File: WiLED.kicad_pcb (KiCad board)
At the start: 2 copper layers, 36.6 x 82.3 mm, 54 parts, among them P1 Serial to USB, P2 DC In, P3 Lamp Connector, P4 LED Out, SW1 Reset, SW2 Boot, SW3 Toggle, SW4 Rotary Encoder, U1 ESP-WROOM-32, U2 VXO7803-500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

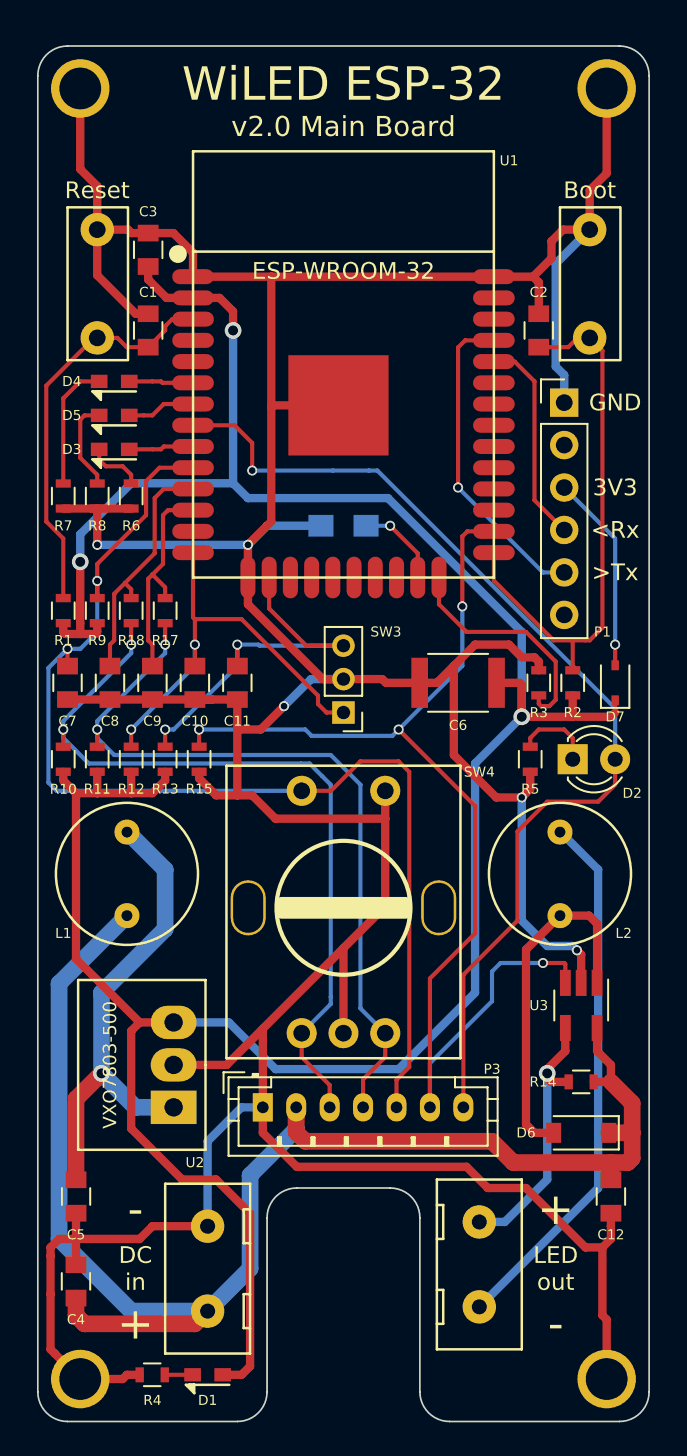
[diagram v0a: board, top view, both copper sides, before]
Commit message: Add ground copper pours
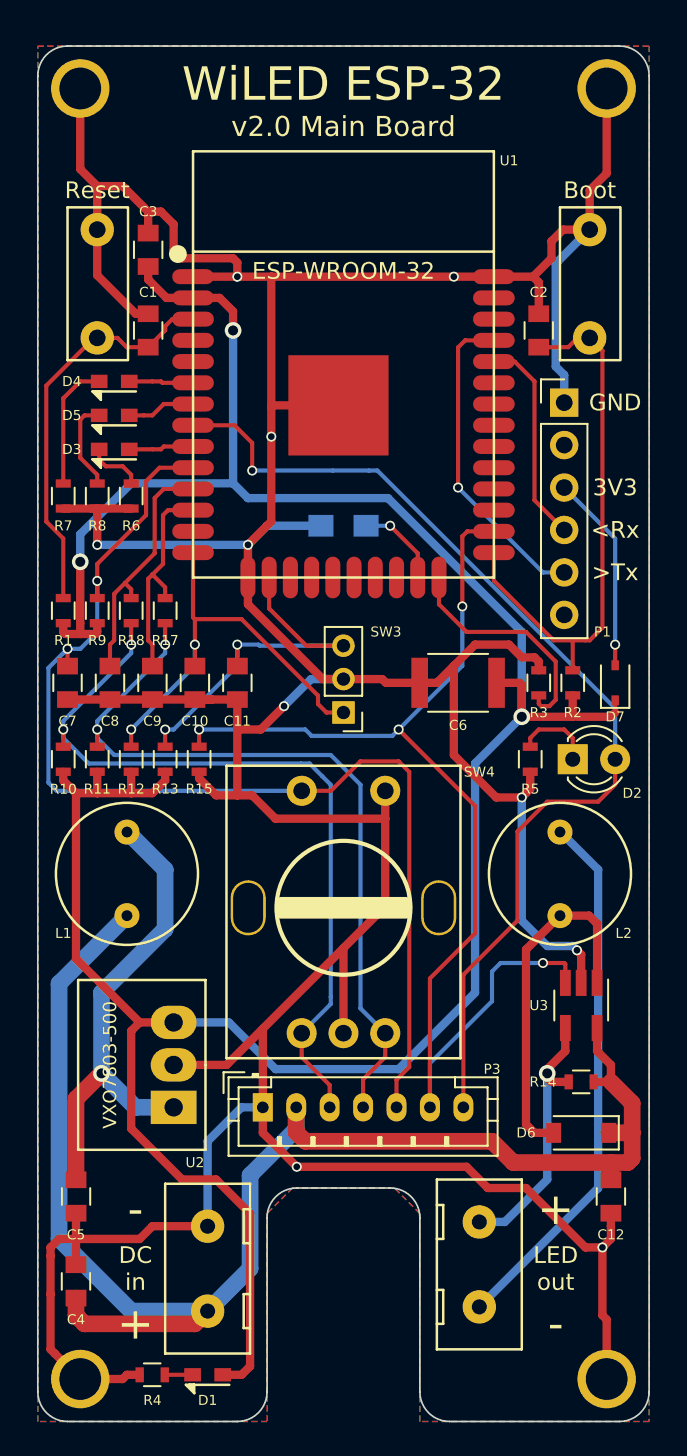
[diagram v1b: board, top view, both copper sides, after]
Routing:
- net GND: track 303.1 -> 308.8 mm, vias 5 -> 10
- added copper zone on B.Cu, net GND
- added copper zone on F.Cu, net GND
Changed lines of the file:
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@@
     (links 107)
     (no_connects 0)
-    (area 152.733905 50.414 193.25362 135.868)
+    (area 154.381999 52.019999 191.058001 134.416001)
     (thickness 1.6)
     (drawings 36)
-    (tracks 493)
+    (tracks 509)
     (zones 0)
     (modules 54)
@@
     (trace_clearance 0.25)
     (zone_clearance 0.508)
-    (zone_45_only no)
+    (zone_45_only yes)
     (trace_min 0.25)
     (segment_width 0.2)
@@
     (pad_drill 2.5)
     (pad_to_mask_clearance 0)
-    (aux_axis_origin 0 0)
+    (aux_axis_origin 154.432 52.07)
     (visible_elements FFFFFF7F)
     (pcbplotparams
-      (layerselection 0x00030_80000001)
-      (usegerberextensions false)
+      (layerselection 0x010f8_80000001)
+      (usegerberextensions true)
       (excludeedgelayer true)
       (linewidth 0.100000)
@@
       (outputformat 1)
       (mirror false)
-      (drillshape 1)
+      (drillshape 0)
       (scaleselection 1)
-      (outputdirectory ""))
+      (outputdirectory gerber/))
   )
   (net 0 "")
@@
   (segment (start 162.052 68.834) (end 162.052 69.072) (width 0.25) (layer F.Cu) (net 1))
   (segment (start 162.052 69.072) (end 161.036 70.088) (width 0.25) (layer F.Cu) (net 1))
+  (via (at 166.37 65.87) (size 0.6) (drill 0.4) (layers F.Cu B.Cu) (net 2))
+  (segment (start 166.3446 65.913) (end 166.3446 65.8954) (width 0.5) (layer B.Cu) (net 2))
+  (segment (start 166.3446 65.8954) (end 166.37 65.87) (width 0.5) (layer B.Cu) (net 2))
+  (via (at 179.324 65.87) (size 0.6) (drill 0.4) (layers F.Cu B.Cu) (net 2))
+  (segment (start 179.2986 65.8368) (end 179.2986 65.8446) (width 0.5) (layer B.Cu) (net 2))
+  (segment (start 179.2986 65.8446) (end 179.324 65.87) (width 0.5) (layer B.Cu) (net 2))
+  (via (at 168.402 75.438) (size 0.6) (drill 0.4) (layers F.Cu B.Cu) (net 2))
+  (via (at 169.926 119.126) (size 0.6) (drill 0.4) (layers F.Cu B.Cu) (net 2))
+  (via (at 188.214 123.952) (size 0.6) (drill 0.4) (layers F.Cu B.Cu) (net 2))
+  (segment (start 166.37 65.87) (end 166.37 65.024) (width 0.5) (layer F.Cu) (net 2))
+  (segment (start 161.798 61.976) (end 161.036 61.976) (width 0.5) (layer F.Cu) (net 2))
+  (segment (start 162.56 62.738) (end 161.798 61.976) (width 0.5) (layer F.Cu) (net 2))
+  (segment (start 162.56 64.262) (end 162.56 62.738) (width 0.5) (layer F.Cu) (net 2))
+  (segment (start 163.068 64.77) (end 162.56 64.262) (width 0.5) (layer F.Cu) (net 2))
+  (segment (start 166.116 64.77) (end 163.068 64.77) (width 0.5) (layer F.Cu) (net 2))
+  (segment (start 166.37 65.024) (end 166.116 64.77) (width 0.5) (layer F.Cu) (net 2))
+  (segment (start 161.036 63.262) (end 161.036 61.976) (width 0.5) (layer F.Cu) (net 2))
+  (segment (start 159.512 60.452) (end 157.988 60.452) (width 0.5) (layer F.Cu) (net 2))
+  (segment (start 161.036 61.976) (end 159.512 60.452) (width 0.5) (layer F.Cu) (net 2))
   (segment (start 187.452 63.0555) (end 187.452 60.706) (width 0.5) (layer F.Cu) (net 2))
   (segment (start 188.468 59.69) (end 188.468 54.61) (width 0.5) (layer F.Cu) (net 2))
@@
   (segment (start 172.72 106.045) (end 172.72 111.132) (width 0.5) (layer F.Cu) (net 2))
   (segment (start 167.005 83.87) (end 167.005 81.915) (width 0.5) (layer F.Cu) (net 2))
-  (segment (start 168.402 80.518) (end 168.402 73.66) (width 0.5) (layer F.Cu) (net 2))
+  (segment (start 168.402 80.518) (end 168.402 75.438) (width 0.5) (layer F.Cu) (net 2))
+  (segment (start 168.402 75.438) (end 168.402 73.66) (width 0.5) (layer F.Cu) (net 2))
   (segment (start 168.402 73.66) (end 168.402 65.87) (width 0.5) (layer F.Cu) (net 2))
   (segment (start 167.005 81.915) (end 168.402 80.518) (width 0.5) (layer F.Cu) (net 2))
@@
   (segment (start 157.988 65.786) (end 157.988 63.0555) (width 0.5) (layer F.Cu) (net 2))
   (segment (start 160.29 68.088) (end 157.988 65.786) (width 0.5) (layer F.Cu) (net 2))
-  (segment (start 161.036 63.262) (end 162.544 63.262) (width 0.5) (layer F.Cu) (net 2))
-  (segment (start 163.72 64.438) (end 163.72 65.87) (width 0.5) (layer F.Cu) (net 2))
-  (segment (start 162.544 63.262) (end 163.72 64.438) (width 0.5) (layer F.Cu) (net 2))
-  (segment (start 161.036 63.262) (end 160.036 63.262) (width 0.5) (layer F.Cu) (net 2))
-  (segment (start 159.8295 63.0555) (end 157.988 63.0555) (width 0.5) (layer F.Cu) (net 2))
-  (segment (start 160.036 63.262) (end 159.8295 63.0555) (width 0.5) (layer F.Cu) (net 2))
   (segment (start 181.72 65.87) (end 184.066 65.87) (width 0.5) (layer F.Cu) (net 2))
   (segment (start 185.8645 63.0555) (end 187.706 63.0555) (width 0.5) (layer F.Cu) (net 2))
@@
   (segment (start 185.166 64.77) (end 185.166 63.754) (width 0.5) (layer F.Cu) (net 2))
   (segment (start 184.066 65.87) (end 185.166 64.77) (width 0.5) (layer F.Cu) (net 2))
-  (segment (start 163.72 65.87) (end 168.402 65.87) (width 0.5) (layer F.Cu) (net 2))
-  (segment (start 168.402 65.87) (end 181.72 65.87) (width 0.5) (layer F.Cu) (net 2))
+  (segment (start 163.72 65.87) (end 166.37 65.87) (width 0.5) (layer F.Cu) (net 2))
+  (segment (start 166.37 65.87) (end 168.402 65.87) (width 0.5) (layer F.Cu) (net 2))
+  (segment (start 168.402 65.87) (end 179.324 65.87) (width 0.5) (layer F.Cu) (net 2))
+  (segment (start 179.324 65.87) (end 181.72 65.87) (width 0.5) (layer F.Cu) (net 2))
   (segment (start 157.988 79.744) (end 160.02 79.744) (width 0.5) (layer F.Cu) (net 2))
   (segment (start 155.956 79.744) (end 157.988 79.744) (width 0.5) (layer F.Cu) (net 2))
@@
   (segment (start 175.22 111.085) (end 175.22 111.132) (width 0.25) (layer B.Cu) (net 51))
   (segment (start 175.22 111.132) (end 175.22 111.085) (width 0.25) (layer B.Cu) (net 51))
+  (zone (net 0) (net_name "") (layer F.Cu) (hatch edge 0.508)
+    (connect_pads (clearance 0.508))
+    (min_thickness 0.254)
+    (keepout (tracks not_allowed) (vias not_allowed) (copperpour not_allowed))
+    (fill (arc_segments 16) (thermal_gap 0.508) (thermal_bridge_width 0.508))
+    (polygon
+      (pts
+        (xy 182.118 64.516) (xy 163.322 64.516) (xy 163.322 52.578) (xy 182.118 52.578)
+      )
+    )
+  )
+  (zone (net 0) (net_name "") (layer B.Cu) (hatch edge 0.508)
+    (connect_pads (clearance 0.508))
+    (min_thickness 0.254)
+    (keepout (tracks not_allowed) (vias not_allowed) (copperpour not_allowed))
+    (fill (arc_segments 16) (thermal_gap 0.508) (thermal_bridge_width 0.508))
+    (polygon
+      (pts
+        (xy 182.118 64.516) (xy 163.322 64.516) (xy 163.322 52.578) (xy 182.118 52.578)
+      )
+    )
+  )
+  (zone (net 2) (net_name GND) (layer B.Cu) (hatch edge 0.508)
+    (connect_pads yes (clearance 0.508))
+    (min_thickness 0.254)
+    (fill yes (arc_segments 32) (thermal_gap 0.508) (thermal_bridge_width 0.508) (smoothing chamfer))
+    (polygon
+      (pts
+        (xy 191.008 134.366) (xy 177.292 134.366) (xy 177.292 121.92) (xy 175.768 120.396) (xy 169.672 120.396)
+        (xy 168.148 121.92) (xy 168.148 134.366) (xy 154.432 134.366) (xy 154.432 52.07) (xy 191.008 52.07)
+      )
+    )
+  )
+  (zone (net 2) (net_name GND) (layer F.Cu) (hatch edge 0.508)
+    (connect_pads yes (clearance 0.508))
+    (min_thickness 0.254)
+    (fill yes (arc_segments 32) (thermal_gap 0.508) (thermal_bridge_width 0.508) (smoothing chamfer))
+    (polygon
+      (pts
+        (xy 191.008 134.366) (xy 177.292 134.366) (xy 177.292 121.92) (xy 175.768 120.396) (xy 169.672 120.396)
+        (xy 168.148 121.92) (xy 168.148 134.366) (xy 154.432 134.366) (xy 154.432 52.07) (xy 191.008 52.07)
+      )
+    )
+  )
 )

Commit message: Increase via size and mounting hole size
Vias were 0.4/0.6 mm, this has been increased to 0.4/0.8 mm to make
manufacturing a little easier - and there's no reason to need the
smaller size.
The mounting holes were M2.5 size, but changed this to M3 for slightly
more standard screw fittings.
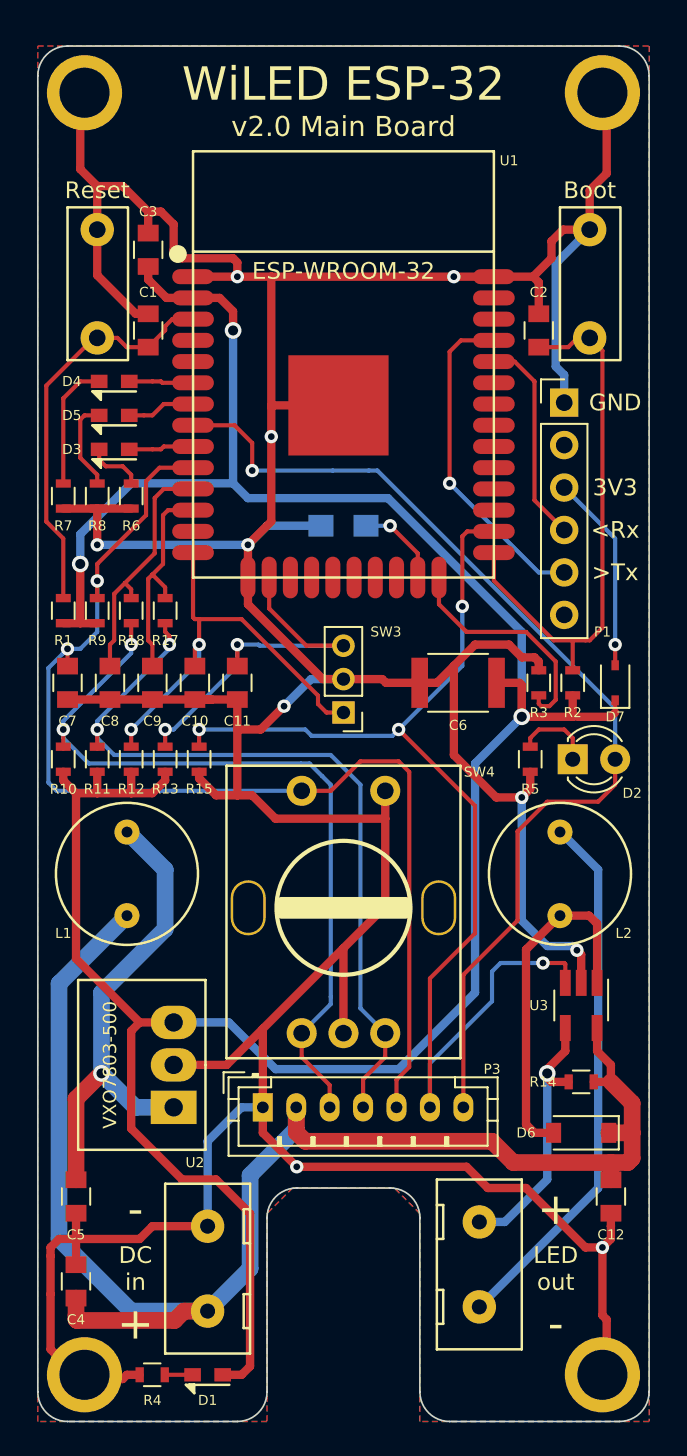
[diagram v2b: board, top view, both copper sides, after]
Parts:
- REF** (x4): footprint custom-footprints:M2.5_hole -> custom-footprints:M3_hole
- moved REF** 0.36 mm to (188.2, 54.9)
- moved REF** 0.36 mm to (157.2, 54.9)
- moved REF** 0.36 mm to (157.2, 131.6)
- moved REF** 0.36 mm to (188.2, 131.6)
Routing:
- net +3V3: track 166.9 -> 165.1 mm
- net TX: track 19.2 -> 19.9 mm
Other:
- net class Default: via_dia 0.6 -> 0.8
- net class GND: via_dia 0.6 -> 0.8
- rule via_min_drill: 0.3 -> 0.4
- rule via_min_size: 0.4 -> 0.7

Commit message: Rework LED constant-current PCB layout
Previously there were unnecssarily long traces between high-power
components in the buck-mode LED driver, this commit brings a modified
layout that tries to improve on this.
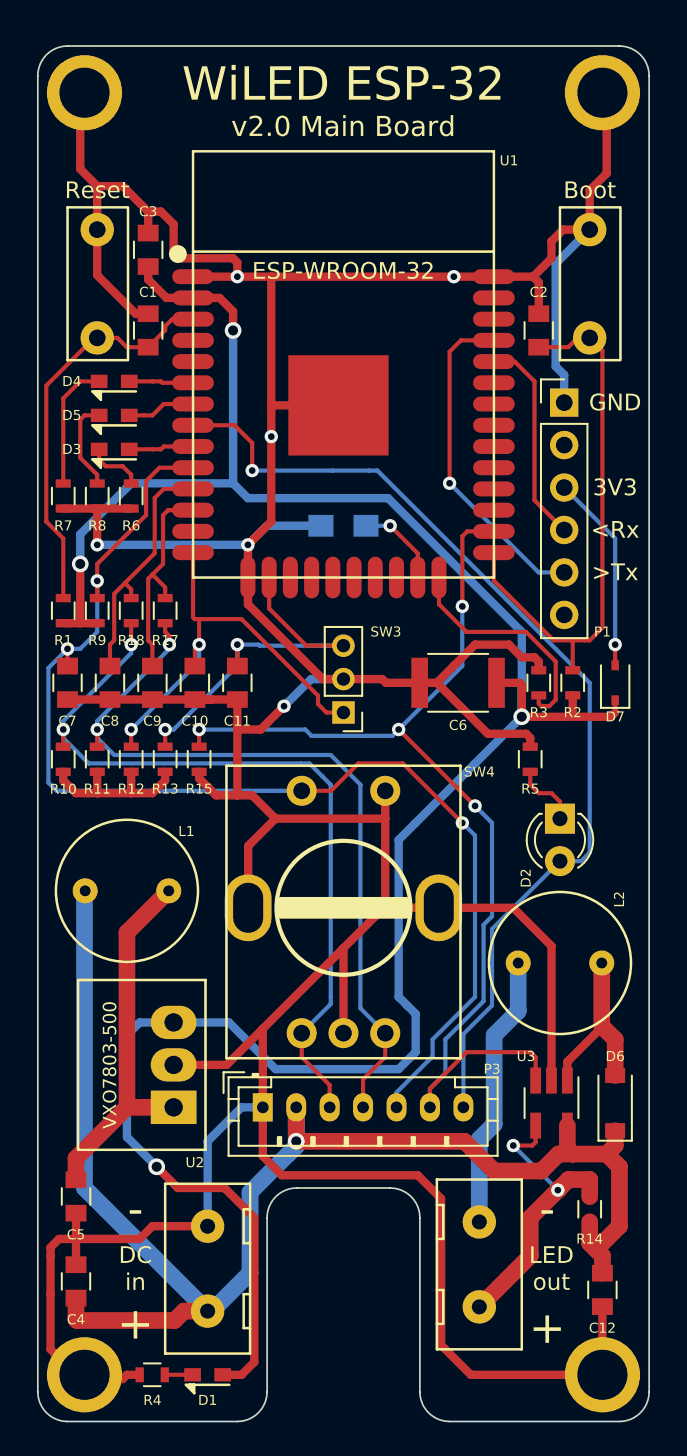
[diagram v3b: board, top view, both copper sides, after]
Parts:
- moved R14 7.64 mm to (187.5, 121.7), turned to 270 degrees
- moved U3 6.11 mm to (185.2, 115.3)
- moved C12 5.61 mm to (188.2, 126.5)
- moved L2 5.33 mm to (185.7, 106.9), turned to 180 degrees
- moved D2 3.64 mm to (185.7, 98.3), turned to 270 degrees
- moved D6 2.70 mm to (189.0, 115.3), turned to 90 degrees
- moved L1 1.02 mm to (159.8, 102.6), turned to 0 degrees
- turned R5 to 270 degrees
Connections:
- P4 pad 1: LED_NEG -> LED_POS
- P4 pad 2: LED_POS -> LED_NEG
- SW4 pad : (no net) -> GND
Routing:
- net LED_NEG: track 32.3 -> 16.5 mm
- net +3V3: track 165.1 -> 151.5 mm, vias 3 -> 4
- net Net-(D6-Pad2): track 21.2 -> 11.2 mm
- net GND: track 308.8 -> 318.5 mm, vias 10 -> 6
- net Net-(C5-Pad1): track 29.1 -> 22.4 mm, vias 1 -> 0
- net LED_PWM: track 69.5 -> 65.2 mm
- net ENC_SW: track 69.3 -> 72.5 mm, vias 2 -> 3
- net LED_POS: track 16.3 -> 19.0 mm, vias 1 -> 2
- net RAW: track 90.1 -> 87.7 mm, vias 0 -> 1
- net IND_PWM: track 62.7 -> 60.4 mm
- net Net-(D2-Pad1): track 4.75 -> 3.99 mm
- removed copper zone on B.Cu, net GND
- removed copper zone on F.Cu, net GND
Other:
- net class POWER: clearance 0.5 -> 0.25

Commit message: Tidy up board outline and improve ground planes
Revised the board outline to make it a nice metric multiple.
Also rerouted some traces to give a more contiguous ground plane.
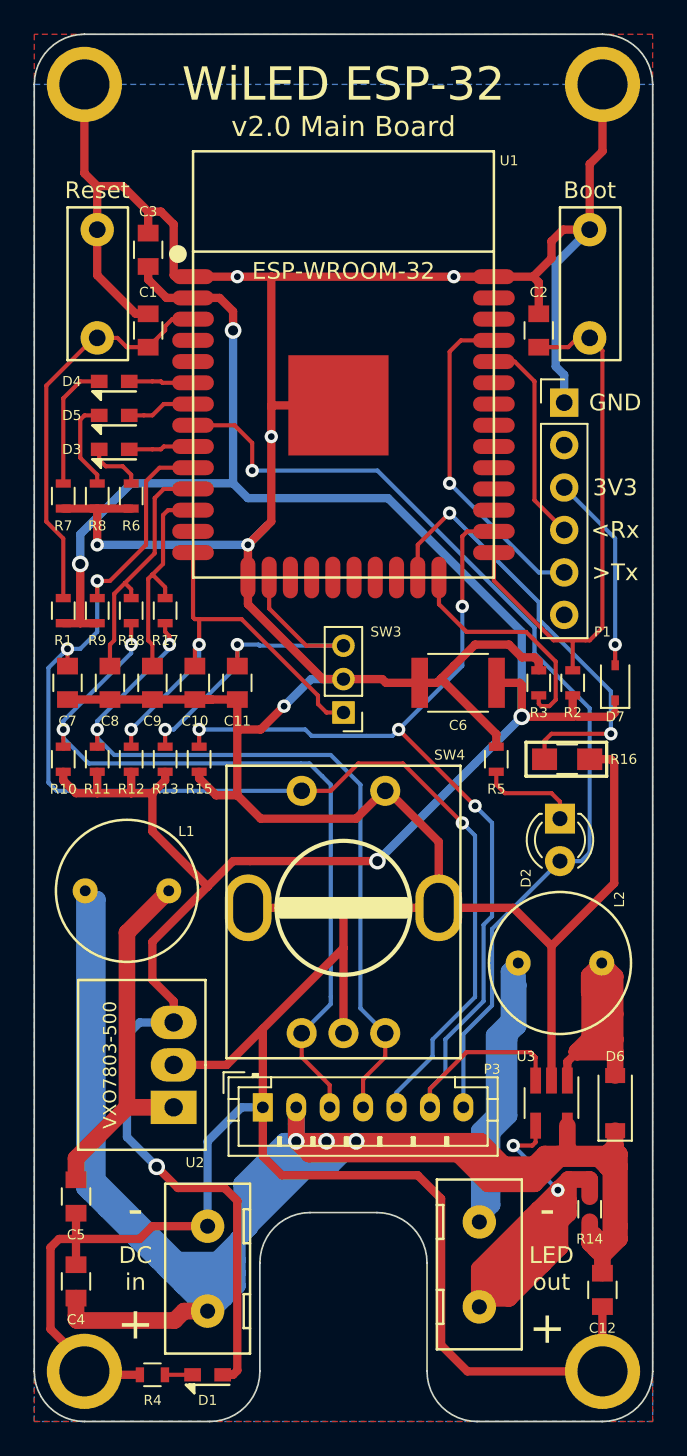
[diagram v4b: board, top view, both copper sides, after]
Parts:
- R16: moved to F.Cu
- moved R16 19.3 mm to (186.1, 94.7), turned to 0 degrees
- moved R5 2.03 mm to (181.9, 94.7)
- moved REF** 0.50 mm to (188.2, 54.4)
- moved REF** 0.50 mm to (157.2, 54.4)
- moved REF** 0.21 mm to (157.2, 131.4)
- moved REF** 0.21 mm to (188.2, 131.4)
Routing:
- net RAW: track 87.7 -> 199.6 mm, vias 1 -> 3
- net LED_POS: track 19.0 -> 48.8 mm
- net Net-(R16-Pad1): track 5.23 -> 27.1 mm, vias 1 -> 2
- net LED_NEG: track 16.5 -> 32.2 mm
- net Net-(D6-Pad2): track 11.2 -> 25.3 mm
- net GND: track 318.5 -> 327.7 mm
- net Net-(D2-Pad1): track 3.99 -> 6.02 mm
- net +3V3: track 151.5 -> 150.8 mm, vias 4 -> 5
- added copper zone on B.Cu, net GND
- added copper zone on F.Cu, net GND
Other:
- board size 36.6 x 82.3 mm -> 37 x 83 mm
